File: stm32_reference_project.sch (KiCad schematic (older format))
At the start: 38 parts, among them J1 USB_Serial, J2 PROG_HDR, SW1 RESET, SW2 BOOT_SELECT, SW3 BAT_SELECT, U2 STM32F103C8Tx, Y1 8Mhz, Y2 32.768K

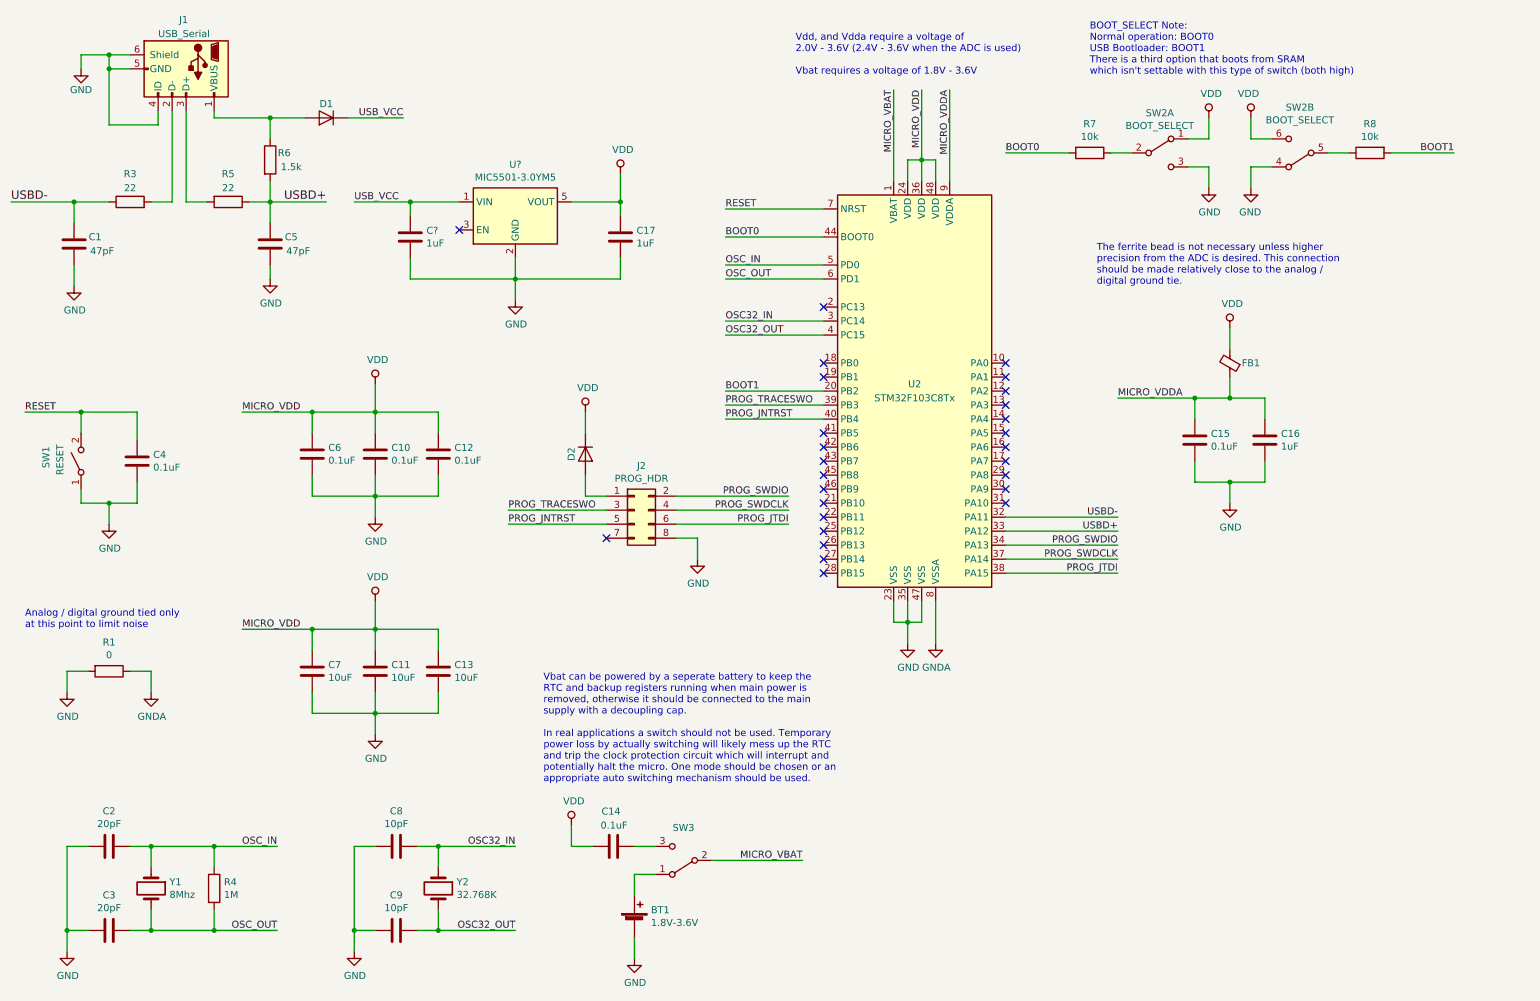
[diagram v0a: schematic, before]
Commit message: progress on the reference schematic
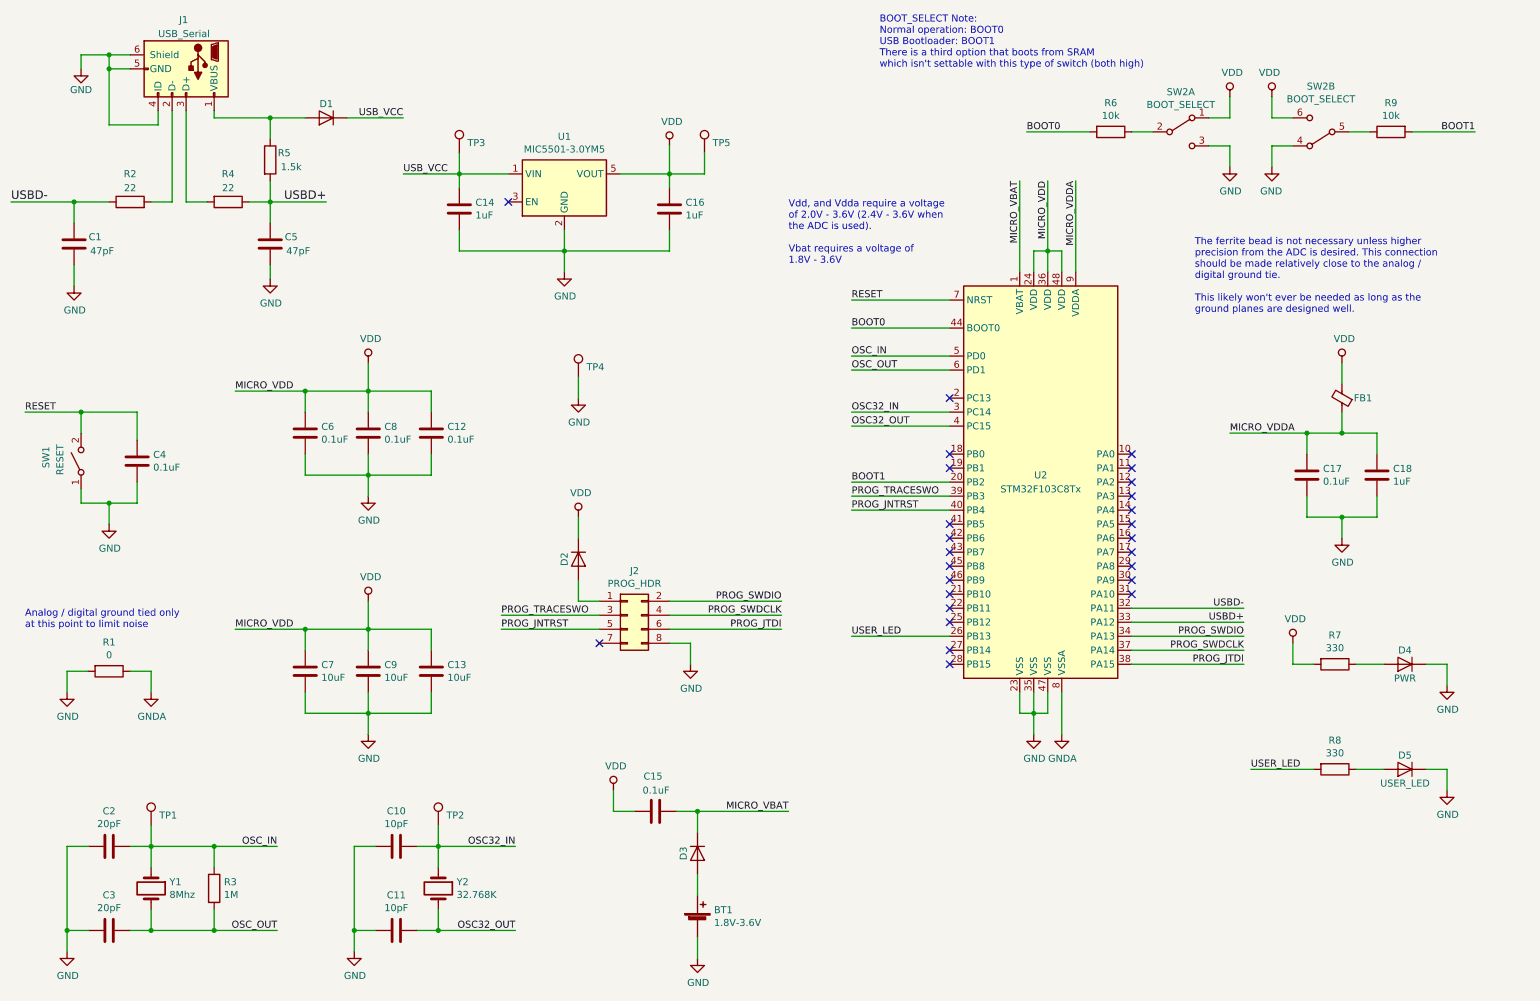
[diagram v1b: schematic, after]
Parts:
- removed SW3: BAT_SELECT, Button_Switch_SMD:SW_SPDT_CK-JS102011SAQN, symbol Switch:SW_SPDT
- added D3: 12V, Diode_SMD:D_SOD-123, symbol Device:D
- added D4, D5: RED, Diode_SMD:D_0603_1608Metric, symbol Device:D
- added R7, R8: 330, Resistor_SMD:R_0603_1608Metric, symbol Device:R
- added TP1: HSE Clock, TestPoint:TestPoint_Pad_D1.5mm, symbol Connector:TestPoint
- added TP2: LSI Clock, TestPoint:TestPoint_Pad_D1.5mm, symbol Connector:TestPoint
- added TP3: Incoming Power, TestPoint:TestPoint_Pad_D1.5mm, symbol Connector:TestPoint
- added TP4: Reference Ground, TestPoint:TestPoint_Pad_D2.0mm, symbol Connector:TestPoint
- added TP5: Regulated Power, TestPoint:TestPoint_Pad_D1.5mm, symbol Connector:TestPoint
- BT1: footprint Battery:Battery_CR1225 -> Battery:BatteryHolder_MPD_BC2003_1x2032
- C4: footprint (none) -> Capacitor_SMD:C_0603_1608Metric
- D1, D2: value NEEDS_SPEC -> 12V; DigiKey Part (none) -> 1727-7763-1-ND; DigiKey Price (none) -> 0.15
- gave numbers to parts that had none: 2
- renumbered C8 to C10, C9 to C11, C14 to C15, C17 to C16, C15 to C17, C16 to C18, C10 to C8, C11 to C9, R3 to R2, R4 to R3, R5 to R4, R6 to R5, R7 to R6, R8 to R9
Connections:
- net GND: now also D4.1 (K), D5.1 (K), TP4.1
- net MICRO_VBAT: now also C15.2, D3.1 (K)
- net OSC32_IN: now also TP2.1
- net OSC_IN: now also TP1.1
- net USB_VCC: now also TP3.1
- net VDD: now also R7.2, TP5.1
- net USER_LED: now reaches U2.26 (PB13)
- net USER_LED: now also R8.2
- net at BT1.1 (+): now also D3.2 (A)
- new net: D4.2 (A), R7.1
- new net: D5.2 (A), R8.1
- no-connect marks 27 -> 26
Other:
- note added: "The ferrite bead is not necessary unless higher\nprecision from the ADC is desired. This connection\nshould be made relatively close to the analog /\ndigital ground tie.\n\nThis likely won't ever be needed as long as the\nground planes are designed well."
- note added: "Vdd, and Vdda require a voltage\nof 2.0V - 3.6V (2.4V - 3.6V when\nthe ADC is used).\n\nVbat requires a voltage of\n1.8V - 3.6V"
- note removed: "The ferrite bead is not necessary unless higher\nprecision from the ADC is desired. This connection\nshould be made relatively close to the analog /\ndigital ground tie."
- note removed: "Vbat can be powered by a seperate battery to keep the\nRTC and backup registers running when main power is\nremoved, otherwise it should be connected to the main\nsupply with a decoupling cap.\n\nIn real applications a switch should not be used. Temporary\npower loss by actually switching will likely mess up the RTC\nand trip the clock protection circuit which will interrupt and\npotentially halt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"
- note removed: "Vdd, and Vdda require a voltage of\n2.0V - 3.6V (2.4V - 3.6V when the ADC is used)\n\nVbat requires a voltage of 1.8V - 3.6V"
- moved on the sheet: BT1, C12, C13, C14, C15, C16, C17, C18, C6, C7, C8, C9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
